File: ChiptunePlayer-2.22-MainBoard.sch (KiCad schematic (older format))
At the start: 1 part, among them J2 Conn_02x10_Odd_Even

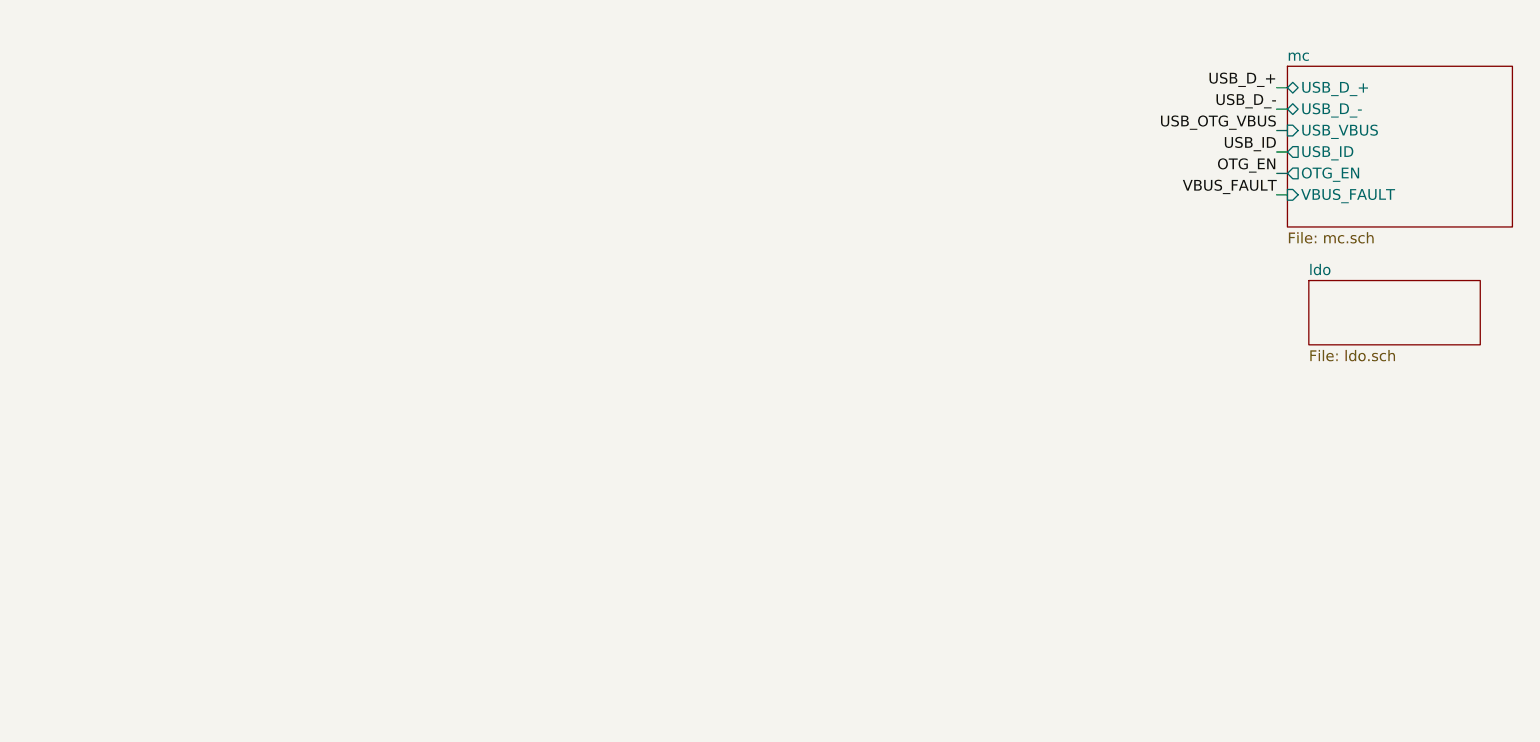
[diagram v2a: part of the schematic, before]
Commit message: Добавил LCD. Уже есть набросок формата платы с экраном и кнопками.
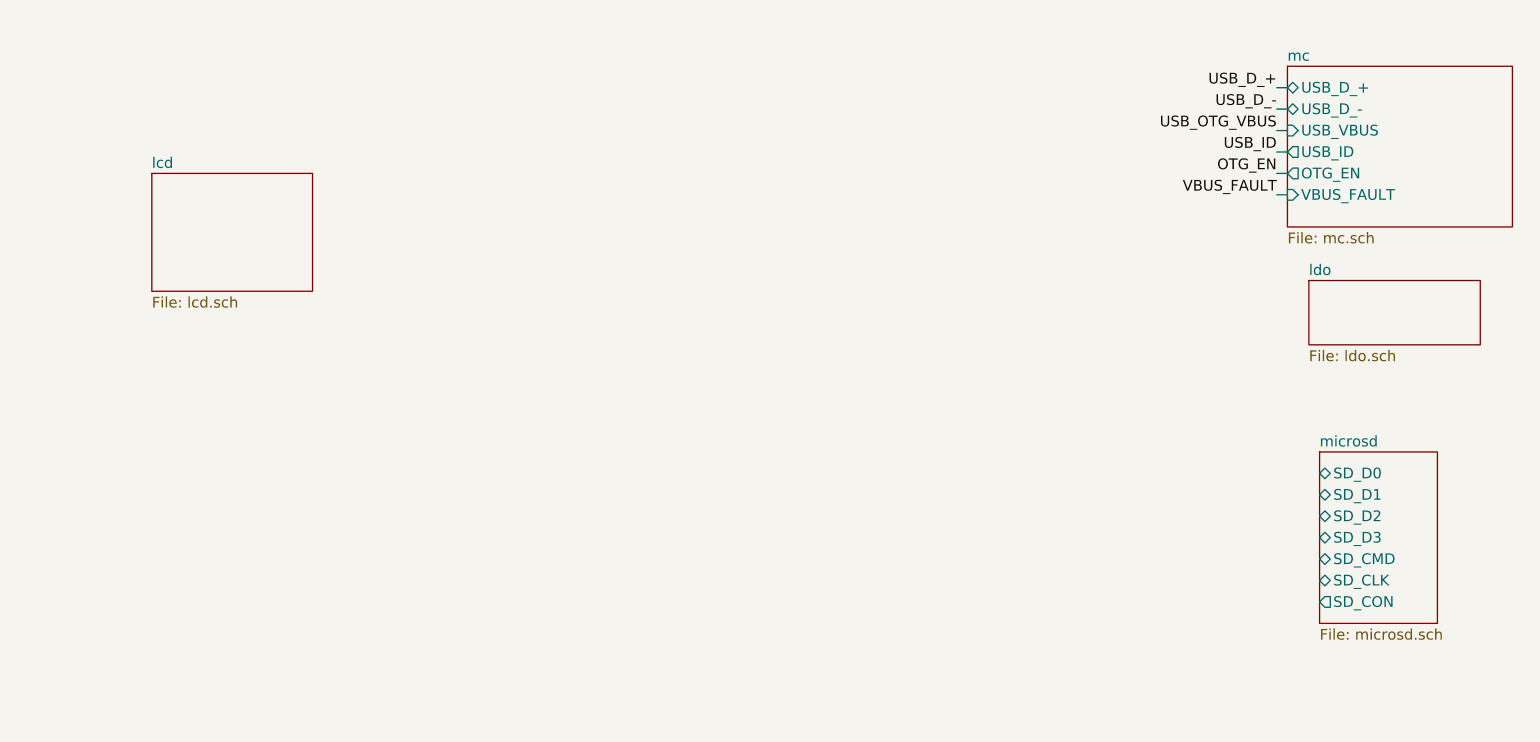
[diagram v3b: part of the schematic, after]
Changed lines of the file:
@@
 $Descr A4 11693 8268
 encoding utf-8
-Sheet 1 9
+Sheet 1 11
 Title ""
 Date "2020-04-18"
@@
 Wire Wire Line
 	8400 3800 8450 3800
+$Sheet
+S 8600 5000 550  800
+U 5ECB9171
+F0 "microsd" 50
+F1 "microsd.sch" 50
+F2 "SD_D2" B L 8600 5300 50
+F3 "SD_D3" B L 8600 5400 50
+F4 "SD_D1" B L 8600 5200 50
+F5 "SD_D0" B L 8600 5100 50
+F6 "SD_CMD" B L 8600 5500 50
+F7 "SD_CLK" B L 8600 5600 50
+F8 "SD_CON" O L 8600 5700 50
+$EndSheet
+$Sheet
+S 3150 3700 750  550
+U 5E9E00DA
+F0 "lcd" 50
+F1 "lcd.sch" 50
+$EndSheet
 $EndSCHEMATC

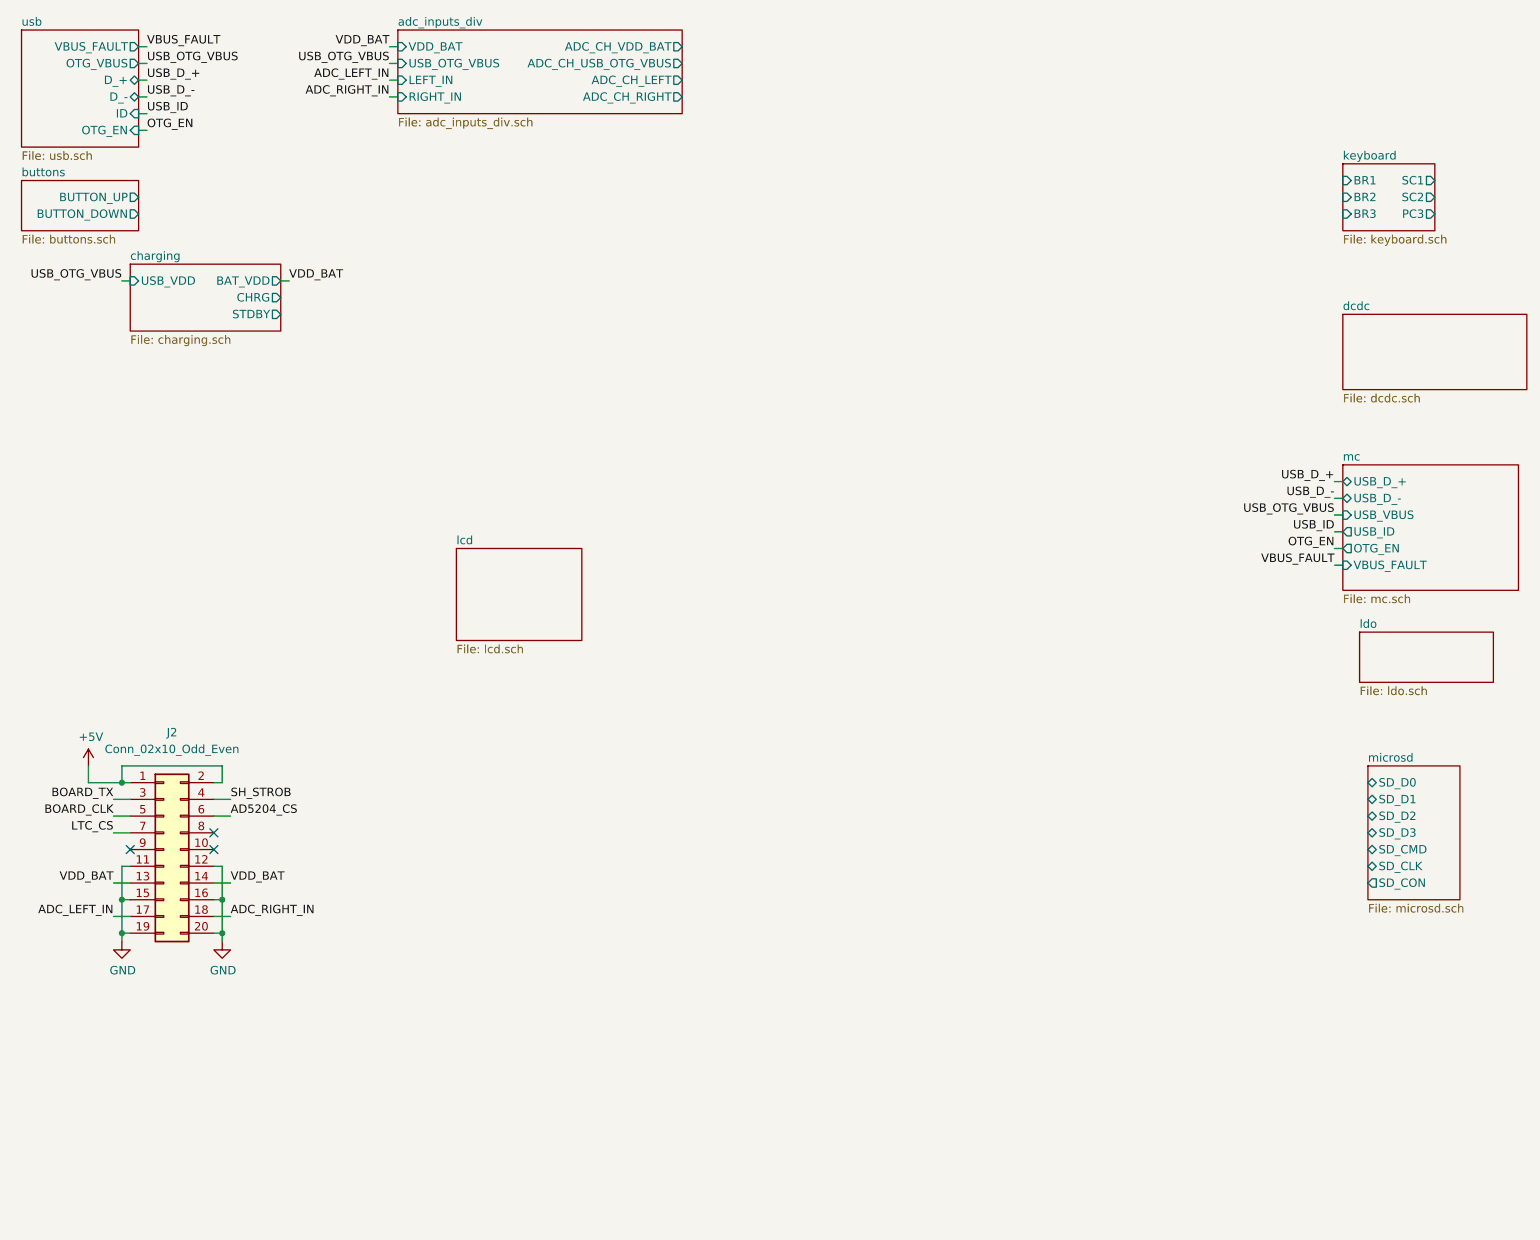
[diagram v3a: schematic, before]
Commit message: dcdc доделан на 5V.
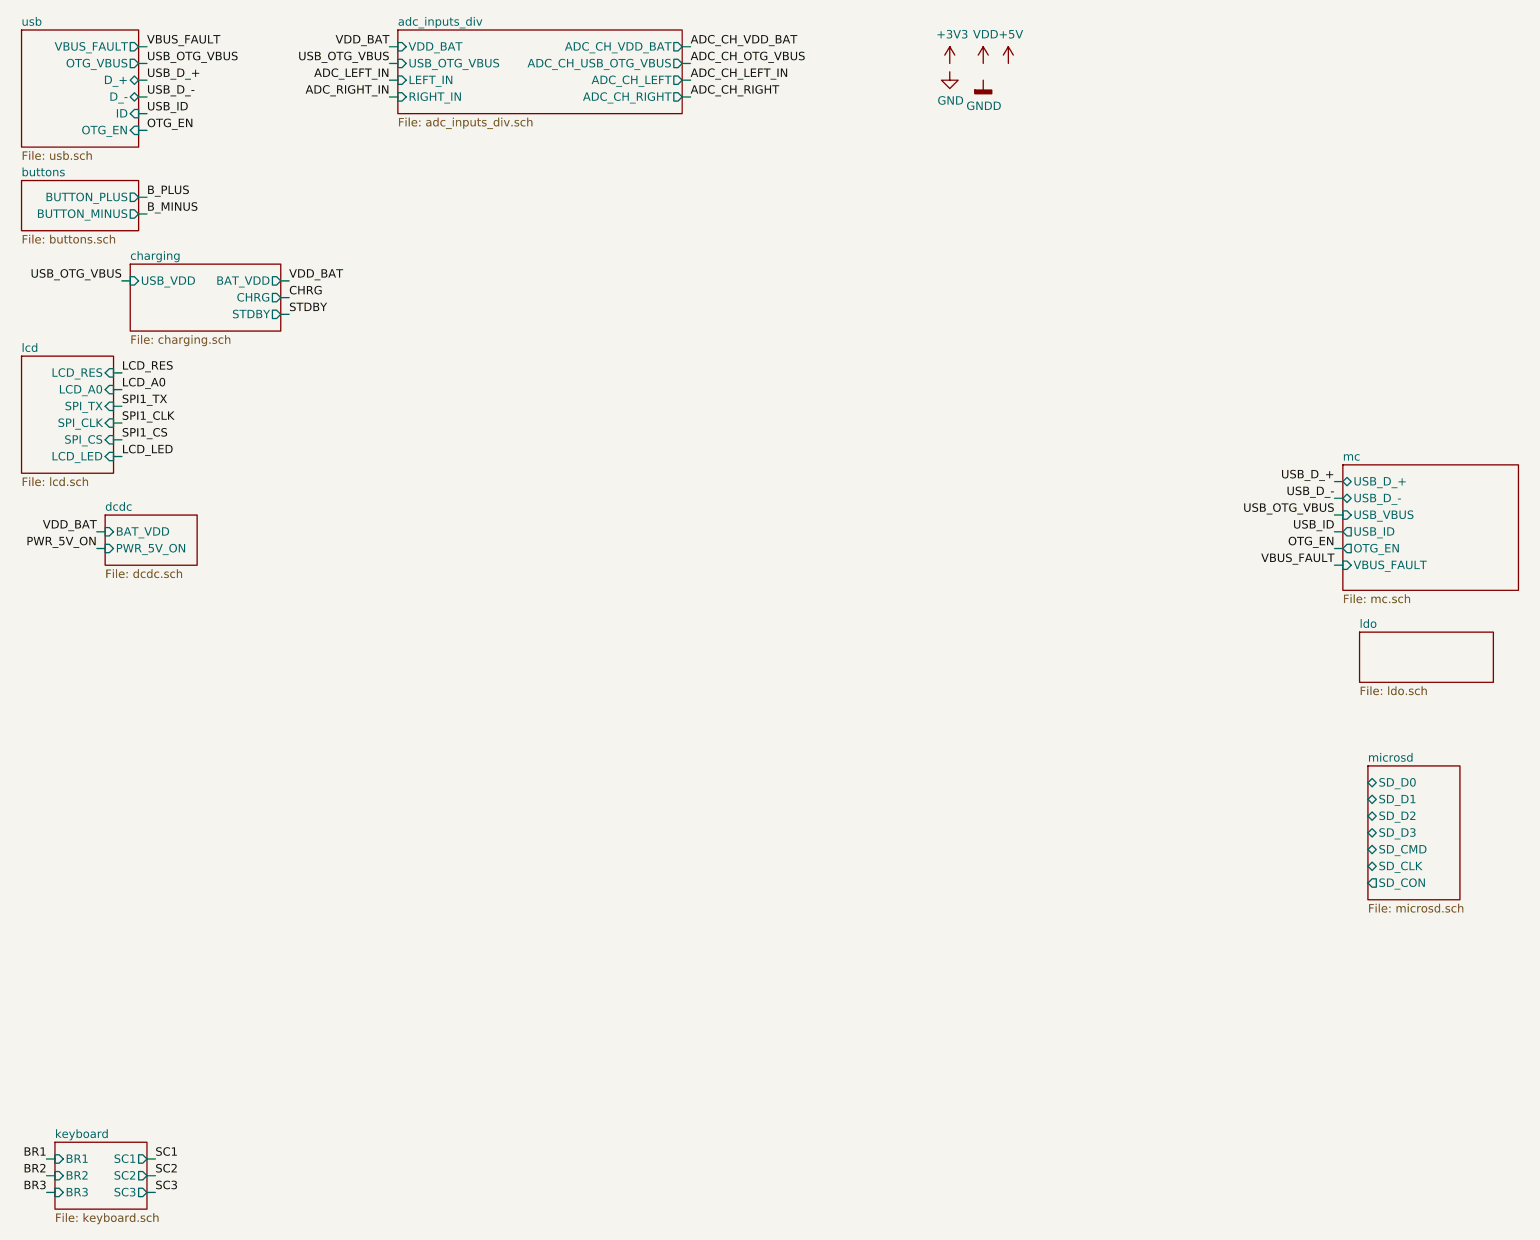
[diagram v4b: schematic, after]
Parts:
- removed J2: Conn_02x10_Odd_Even, Connector_PinHeader_2.54mm:PinHeader_2x10_P2.54mm_Vertical_SMD, symbol Connector_Generic:Conn_02x10_Odd_Even
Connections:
- no-connect marks 3 -> 0
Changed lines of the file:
@@
 Comment4 "Vadimatorik"
 $EndDescr
-$Comp
-L power:+5V #PWR01
-U 1 1 5EABF65B
-P 950 5000
-F 0 "#PWR01" H 950 4850 50  0001 C CNN
-F 1 "+5V" H 965 5173 50  0000 C CNN
-F 2 "" H 950 5000 50  0001 C CNN
-F 3 "" H 950 5000 50  0001 C CNN
-	1    950  5000
-	1    0    0    -1
-$EndComp
-$Comp
-L power:GND #PWR02
-U 1 1 5EAC2A23
-P 1150 6050
-F 0 "#PWR02" H 1150 5800 50  0001 C CNN
-F 1 "GND" H 1155 5877 50  0000 C CNN
-F 2 "" H 1150 6050 50  0001 C CNN
-F 3 "" H 1150 6050 50  0001 C CNN
-	1    1150 6050
-	1    0    0    -1
-$EndComp
 $Sheet
 S 550  1500 700  300
@@
 F0 "buttons" 50
 F1 "buttons.sch" 50
-F2 "BUTTON_UP" O R 1250 1600 50
-F3 "BUTTON_DOWN" O R 1250 1700 50
+F2 "BUTTON_PLUS" O R 1250 1600 50
+F3 "BUTTON_MINUS" O R 1250 1700 50
 $EndSheet
 $Sheet
@@
 F9 "ADC_CH_RIGHT" O R 4500 1000 50
 $EndSheet
-$Comp
-L Connector_Generic:Conn_02x10_Odd_Even J2
-U 1 1 5EA4935C
-P 1400 5500
-F 0 "J2" H 1450 6200 50  0000 C CNN
-F 1 "Conn_02x10_Odd_Even" H 1450 6100 50  0000 C CNN
-F 2 "Connector_PinHeader_2.54mm:PinHeader_2x10_P2.54mm_Vertical_SMD" H 1400 5500 50  0001 C CNN
-F 3 "~" H 1400 5500 50  0001 C CNN
-	1    1400 5500
-	1    0    0    -1
-$EndComp
-$Comp
-L power:GND #PWR05
-U 1 1 5EA53146
-P 1750 6050
-F 0 "#PWR05" H 1750 5800 50  0001 C CNN
-F 1 "GND" H 1755 5877 50  0000 C CNN
-F 2 "" H 1750 6050 50  0001 C CNN
-F 3 "" H 1750 6050 50  0001 C CNN
-	1    1750 6050
-	1    0    0    -1
-$EndComp
-Wire Wire Line
-	1200 5100 1150 5100
-Wire Wire Line
-	950  5100 950  5000
-Wire Wire Line
-	1700 5100 1750 5100
-Wire Wire Line
-	1750 5100 1750 5000
-Wire Wire Line
-	1750 5000 1150 5000
-Wire Wire Line
-	1150 5000 1150 5100
-Connection ~ 1150 5100
-Wire Wire Line
-	1150 5100 950  5100
-Wire Wire Line
-	1200 6000 1150 6000
-Wire Wire Line
-	1150 6000 1150 6050
-Wire Wire Line
-	1700 6000 1750 6000
-Wire Wire Line
-	1750 6000 1750 6050
-Wire Wire Line
-	1100 5900 1200 5900
-Wire Wire Line
-	1150 6000 1150 5800
-Wire Wire Line
-	1150 5800 1200 5800
-Connection ~ 1150 6000
-Wire Wire Line
-	1750 6000 1750 5800
-Wire Wire Line
-	1750 5800 1700 5800
-Connection ~ 1750 6000
-Wire Wire Line
-	1700 5900 1800 5900
-Wire Wire Line
-	1700 5200 1800 5200
-Wire Wire Line
-	1700 5300 1800 5300
-Wire Wire Line
-	1100 5200 1200 5200
-Wire Wire Line
-	1100 5300 1200 5300
-Wire Wire Line
-	1100 5400 1200 5400
-Text Label 1800 5200 0    50   ~ 0
-SH_STROB
-Text Label 1800 5300 0    50   ~ 0
-AD5204_CS
-Text Label 1800 5900 0    50   ~ 0
-ADC_RIGHT_IN
-Text Label 1100 5900 2    50   ~ 0
-ADC_LEFT_IN
-Text Label 1100 5400 2    50   ~ 0
-LTC_CS
-Text Label 1100 5300 2    50   ~ 0
-BOARD_CLK
-Text Label 1100 5200 2    50   ~ 0
-BOARD_TX
 Text Label 2750 900  2    50   ~ 0
 ADC_LEFT_IN
@@
 Wire Wire Line
 	2750 700  2800 700
-Text Label 1100 5700 2    50   ~ 0
-VDD_BAT
-Text Label 1800 5700 0    50   ~ 0
-VDD_BAT
-Wire Wire Line
-	1700 5700 1800 5700
-Wire Wire Line
-	1750 5800 1750 5600
-Wire Wire Line
-	1750 5600 1700 5600
-Connection ~ 1750 5800
-Wire Wire Line
-	1100 5700 1200 5700
-Wire Wire Line
-	1150 5800 1150 5600
-Wire Wire Line
-	1150 5600 1200 5600
-Connection ~ 1150 5800
 Text Label 1300 800  0    50   ~ 0
 USB_OTG_VBUS
@@
 Wire Wire Line
 	1150 2100 1200 2100
-NoConn ~ 1700 5400
-NoConn ~ 1700 5500
-NoConn ~ 1200 5500
-$Sheet
-S 8450 2300 1100 450
+$Sheet
+S 1050 3500 550  300
 U 5E9B0FB9
 F0 "dcdc" 50
 F1 "dcdc.sch" 50
+F2 "BAT_VDD" I L 1050 3600 50
+F3 "PWR_5V_ON" I L 1050 3700 50
 $EndSheet
 $Sheet
@@
 $EndSheet
 $Sheet
-S 8450 1400 550  400
+S 750  7250 550  400
 U 5E9B1427
 F0 "keyboard" 50
 F1 "keyboard.sch" 50
-F2 "BR1" I L 8450 1500 50
-F3 "BR2" I L 8450 1600 50
-F4 "BR3" I L 8450 1700 50
-F5 "SC1" O R 9000 1500 50
-F6 "SC2" O R 9000 1600 50
-F7 "PC3" O R 9000 1700 50
+F2 "BR1" I L 750 7350 50
+F3 "BR2" I L 750 7450 50
+F4 "BR3" I L 750 7550 50
+F5 "SC1" O R 1300 7350 50
+F6 "SC2" O R 1300 7450 50
+F7 "SC3" O R 1300 7550 50
 $EndSheet
 Wire Wire Line
@@
 $EndSheet
 $Sheet
-S 3150 3700 750  550
+S 550  2550 550  700
 U 5E9E00DA
 F0 "lcd" 50
 F1 "lcd.sch" 50
-$EndSheet
+F2 "LCD_RES" I R 1100 2650 50
+F3 "LCD_A0" I R 1100 2750 50
+F4 "SPI_TX" I R 1100 2850 50
+F5 "SPI_CLK" I R 1100 2950 50
+F6 "SPI_CS" I R 1100 3050 50
+F7 "LCD_LED" I R 1100 3150 50
+$EndSheet
+$Comp
+L power:+3V3 #PWR?
+U 1 1 5EA4C4B4
+P 6100 800
+AR Path="/5EBBB05A/5EA4C4B4" Ref="#PWR?"  Part="1"
+AR Path="/5EA4C4B4" Ref="#PWR01"  Part="1"
+F 0 "#PWR01" H 6100 650 50  0001 C CNN
+F 1 "+3V3" H 6115 973 50  0000 C CNN
+F 2 "" H 6100 800 50  0001 C CNN
+F 3 "" H 6100 800 50  0001 C CNN
+	1    6100 800
+	1    0    0    -1
+$EndComp
+$Comp
+L power:GND #PWR?
+U 1 1 5EA4C4BA
+P 6100 850
+AR Path="/5EBBB05A/5EA4C4BA" Ref="#PWR?"  Part="1"
+AR Path="/5EA4C4BA" Ref="#PWR02"  Part="1"
+F 0 "#PWR02" H 6100 600 50  0001 C CNN
+F 1 "GND" H 6105 677 50  0000 C CNN
+F 2 "" H 6100 850 50  0001 C CNN
+F 3 "" H 6100 850 50  0001 C CNN
+	1    6100 850
+	1    0    0    -1
+$EndComp
+$Comp
+L power:VDD #PWR?
+U 1 1 5EA506EA
+P 6300 800
+AR Path="/5EB7312D/5EA506EA" Ref="#PWR?"  Part="1"
+AR Path="/5EA506EA" Ref="#PWR05"  Part="1"
+F 0 "#PWR05" H 6300 650 50  0001 C CNN
+F 1 "VDD" H 6315 973 50  0000 C CNN
+F 2 "" H 6300 800 50  0001 C CNN
+F 3 "" H 6300 800 50  0001 C CNN
+	1    6300 800
+	1    0    0    -1
+$EndComp
+$Comp
+L power:GNDD #PWR?
+U 1 1 5EA506F1
+P 6300 900
+AR Path="/5EB7312D/5EA506F1" Ref="#PWR?"  Part="1"
+AR Path="/5EA506F1" Ref="#PWR06"  Part="1"
+F 0 "#PWR06" H 6300 650 50  0001 C CNN
+F 1 "GNDD" H 6304 745 50  0000 C CNN
+F 2 "" H 6300 900 50  0001 C CNN
+F 3 "" H 6300 900 50  0001 C CNN
+	1    6300 900
+	1    0    0    -1
+$EndComp
+Text Label 1300 1600 0    50   ~ 0
+B_PLUS
+Text Label 1300 1700 0    50   ~ 0
+B_MINUS
+Wire Wire Line
+	1300 1600 1250 1600
+Wire Wire Line
+	1250 1700 1300 1700
+Wire Wire Line
+	2100 2200 2150 2200
+Wire Wire Line
+	2100 2300 2150 2300
+Text Label 2150 2200 0    50   ~ 0
+CHRG
+Text Label 2150 2300 0    50   ~ 0
+STDBY
+Wire Wire Line
+	1300 7350 1350 7350
+Wire Wire Line
+	1300 7450 1350 7450
+Wire Wire Line
+	1300 7550 1350 7550
+Wire Wire Line
+	750  7350 700  7350
+Wire Wire Line
+	750  7450 700  7450
+Wire Wire Line
+	750  7550 700  7550
+Text Label 1350 7350 0    50   ~ 0
+SC1
+Text Label 1350 7450 0    50   ~ 0
+SC2
+Text Label 1350 7550 0    50   ~ 0
+SC3
+Text Label 700  7350 2    50   ~ 0
+BR1
+Text Label 700  7450 2    50   ~ 0
+BR2
+Text Label 700  7550 2    50   ~ 0
+BR3
+Text Label 4550 700  0    50   ~ 0
+ADC_CH_VDD_BAT
+Text Label 4550 800  0    50   ~ 0
+ADC_CH_OTG_VBUS
+Text Label 4550 900  0    50   ~ 0
+ADC_CH_LEFT_IN
+Text Label 4550 1000 0    50   ~ 0
+ADC_CH_RIGHT
+Wire Wire Line
+	4550 700  4500 700
+Wire Wire Line
+	4550 800  4500 800
+Wire Wire Line
+	4550 900  4500 900
+Wire Wire Line
+	4550 1000 4500 1000
+Wire Wire Line
+	1100 2650 1150 2650
+Wire Wire Line
+	1100 2750 1150 2750
+Wire Wire Line
+	1100 2850 1150 2850
+Wire Wire Line
+	1100 2950 1150 2950
+Wire Wire Line
+	1100 3050 1150 3050
+Wire Wire Line
+	1150 3150 1100 3150
+Text Label 1150 2650 0    50   ~ 0
+LCD_RES
+Text Label 1150 2750 0    50   ~ 0
+LCD_A0
+Text Label 1150 2850 0    50   ~ 0
+SPI1_TX
+Text Label 1150 2950 0    50   ~ 0
+SPI1_CLK
+Text Label 1150 3050 0    50   ~ 0
+SPI1_CS
+Text Label 1150 3150 0    50   ~ 0
+LCD_LED
+$Comp
+L power:+5V #PWR?
+U 1 1 5EA6B614
+P 6450 800
+AR Path="/5E9B0FB9/5EA6B614" Ref="#PWR?"  Part="1"
+AR Path="/5EA6B614" Ref="#PWR043"  Part="1"
+F 0 "#PWR043" H 6450 650 50  0001 C CNN
+F 1 "+5V" H 6465 973 50  0000 C CNN
+F 2 "" H 6450 800 50  0001 C CNN
+F 3 "" H 6450 800 50  0001 C CNN
+	1    6450 800
+	1    0    0    -1
+$EndComp
+Wire Wire Line
+	1050 3600 1000 3600
+Wire Wire Line
+	1000 3700 1050 3700
+Text Label 1000 3600 2    50   ~ 0
+VDD_BAT
+Text Label 1000 3700 2    50   ~ 0
+PWR_5V_ON
 $EndSCHEMATC

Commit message: Сделал плату компактнее.
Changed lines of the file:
@@
 $Descr A4 11693 8268
 encoding utf-8
-Sheet 1 11
+Sheet 1 12
 Title ""
 Date "2020-04-18"
@@
 Text Label 1000 3700 2    50   ~ 0
 PWR_5V_ON
+$Sheet
+S 4550 5650 1400 900
+U 5EABB8BC
+F0 "generators" 50
+F1 "generators.sch" 50
+$EndSheet
 $EndSCHEMATC
